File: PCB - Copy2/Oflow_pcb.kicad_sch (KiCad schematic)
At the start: 2 parts, among them U1 NodeMCU

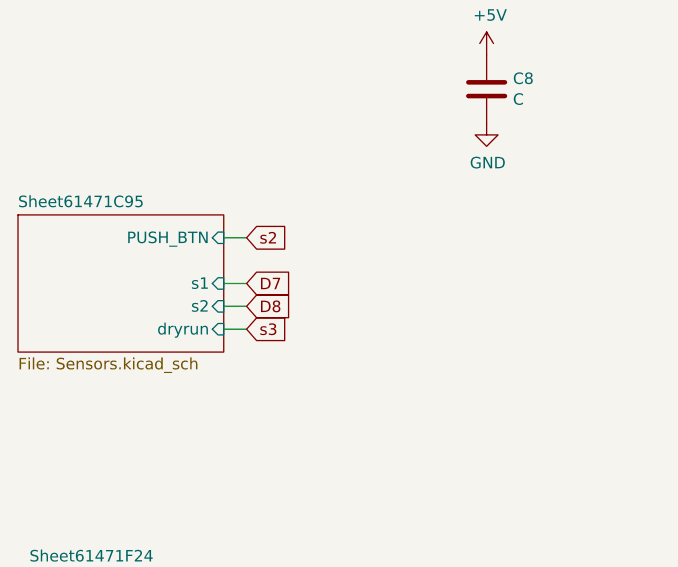
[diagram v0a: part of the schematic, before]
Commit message: nedd to connect ground
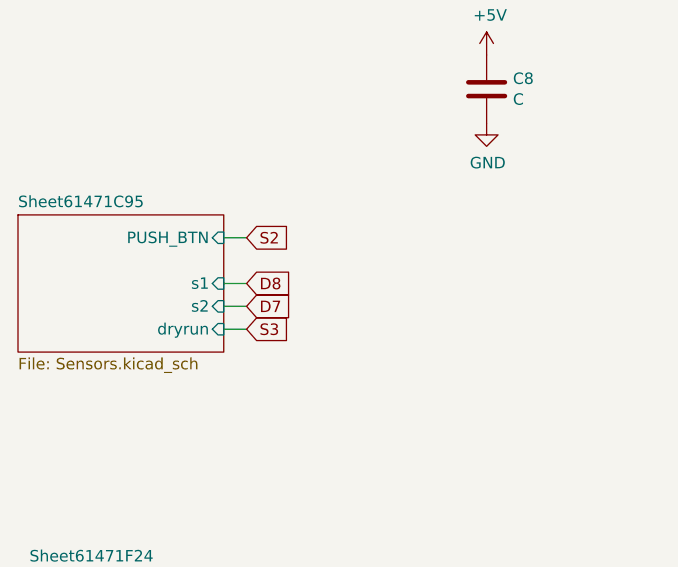
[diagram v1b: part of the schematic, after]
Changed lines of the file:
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@@
     )
   )
-  (global_label "D7" (shape input) (at 59.69 83.82 0) (fields_autoplaced)
+  (global_label "D8" (shape input) (at 59.69 83.82 0) (fields_autoplaced)
     (effects (font (size 1.27 1.27)) (justify left))
     (property "Intersheet References" "${INTERSHEET_REFS}" (id 0) (at 64.4937 83.7406 0)
@@
     )
   )
-  (global_label "D8" (shape input) (at 59.69 86.36 0) (fields_autoplaced)
+  (global_label "D7" (shape input) (at 59.69 86.36 0) (fields_autoplaced)
     (effects (font (size 1.27 1.27)) (justify left))
     (property "Intersheet References" "${INTERSHEET_REFS}" (id 0) (at 64.4937 86.2806 0)
@@
     )
   )
-  (global_label "s2" (shape input) (at 59.69 78.74 0) (fields_autoplaced)
-    (effects (font (size 1.27 1.27)) (justify left))
-    (property "Intersheet References" "${INTERSHEET_REFS}" (id 0) (at 64.2518 78.6606 0)
+  (global_label "S2" (shape input) (at 59.69 78.74 0) (fields_autoplaced)
+    (effects (font (size 1.27 1.27)) (justify left))
+    (property "Intersheet References" "${INTERSHEET_REFS}" (id 0) (at 64.4332 78.6606 0)
       (effects (font (size 1.27 1.27)) (justify left) hide)
     )
@@
     )
   )
-  (global_label "s3" (shape input) (at 59.69 88.9 0) (fields_autoplaced)
-    (effects (font (size 1.27 1.27)) (justify left))
-    (property "Intersheet References" "${INTERSHEET_REFS}" (id 0) (at 64.2518 88.8206 0)
+  (global_label "S3" (shape input) (at 59.69 88.9 0) (fields_autoplaced)
+    (effects (font (size 1.27 1.27)) (justify left))
+    (property "Intersheet References" "${INTERSHEET_REFS}" (id 0) (at 64.4332 88.8206 0)
       (effects (font (size 1.27 1.27)) (justify left) hide)
     )
@@
     )
     (path "/00000000-0000-0000-0000-000061471c96/643d8d48-d6c0-465f-b2f0-8ceb95e35f35"
-      (reference "Q1") (unit 1) (value "BC547") (footprint "Package_TO_SOT_THT:TO-92_Inline")
+      (reference "Q1") (unit 1) (value "BC547") (footprint "Package_TO_SOT_THT:TO-92L_Wide")
     )
     (path "/00000000-0000-0000-0000-000061471fde/00000000-0000-0000-0000-00006148ade3"
